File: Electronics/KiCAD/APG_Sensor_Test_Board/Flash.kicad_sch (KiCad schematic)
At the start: 0 parts

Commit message: added flash schematic
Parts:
- added C3: C, symbol Device:C
- added R2: 0, symbol Device:R
- added U?: W25Q128JVS, Package_SO:SOIC-8_5.23x5.23mm_P1.27mm, symbol Memory_Flash:W25Q128JVS
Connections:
- new net +3.3V: R2.1
- new net FCLK: U?.6 (CLK)
- new net FCS: U?.1 (~{CS})
- new net FMISO: U?.2 (DO(IO1))
- new net FMOSI: U?.5 (DI(IO0))
- new net FPWR: C3.1, R2.2, U?.3 (IO2), U?.7 (IO3), U?.8 (VCC)
- new net GND: C3.2, U?.4 (GND)

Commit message: Cleaning up schematics
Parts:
- C3: value C -> 1u
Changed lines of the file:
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@@
 			)
 		)
-		(property "Value" "C"
+		(property "Value" "1u"
 			(at 140.97 54.6099 0)
 			(effects

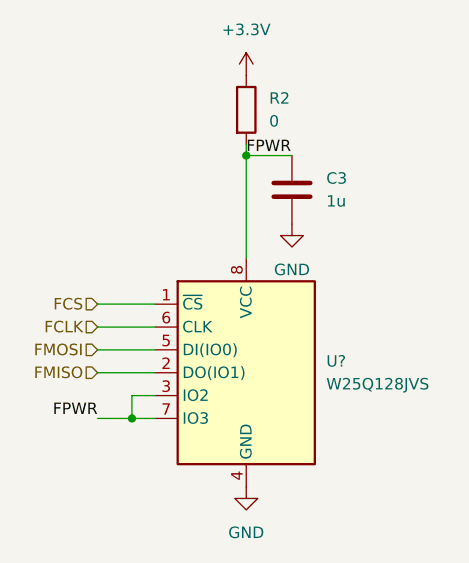
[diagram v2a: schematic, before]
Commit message: Gannon inspection decision to change IMU
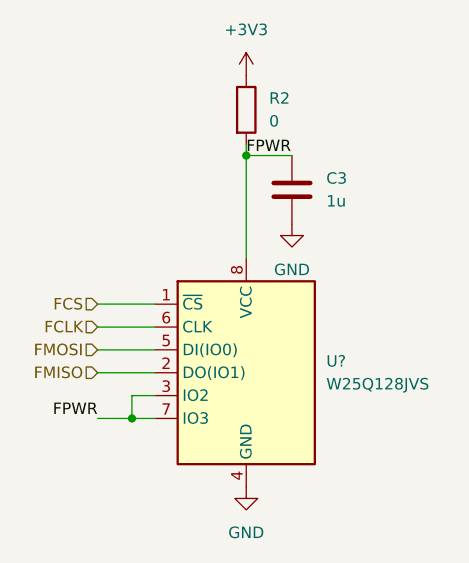
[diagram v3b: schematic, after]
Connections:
- net +3.3V renamed +3V3
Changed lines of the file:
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@@
-	)
-	(symbol
-		(lib_id "power:+3.3V")
-		(at 132.08 40.64 0)
-		(unit 1)
-		(exclude_from_sim no)
-		(in_bom yes)
-		(on_board yes)
-		(dnp no)
-		(fields_autoplaced yes)
-		(property "Reference" "#PWR03"
-			(at 132.08 44.45 0)
-			(effects
-				(font
-					(size 1.27 1.27)
-				)
-				(hide yes)
-			)
-		)
-		(property "Value" "+3.3V"
-			(at 132.08 35.56 0)
-			(effects
-				(font
-					(size 1.27 1.27)
-				)
-			)
-		)
-		(property "Footprint" ""
-			(at 132.08 40.64 0)
-			(effects
-				(font
-					(size 1.27 1.27)
-				)
-				(hide yes)
-			)
-		)
-		(property "Datasheet" ""
-			(at 132.08 40.64 0)
-			(effects
-				(font
-					(size 1.27 1.27)
-				)
-				(hide yes)
-			)
-		)
-		(property "Description" "Power symbol creates a global label with name \"+3.3V\""
-			(at 132.08 40.64 0)
-			(effects
-				(font
-					(size 1.27 1.27)
-				)
-				(hide yes)
-			)
-		)
-		(pin "1"
-		)
-		(instances
-			(project ""
-				(path "/3161be0c-372f-463d-be0a-bab00f344057/1176df13-1d31-4c0d-ab61-bd75d7380dc4"
-					(reference "#PWR03")
-					(unit 1)
-				)
-			)
-		)
 	)
 	(symbol
@@
 					(unit 1)
 				)
+			)
+		)
+	)
+	(symbol
+		(lib_id "power:+3V3")
+		(at 132.08 40.64 0)
+		(unit 1)
+		(exclude_from_sim no)
+		(in_bom yes)
+		(on_board yes)
+		(dnp no)
+		(fields_autoplaced yes)
+		(property "Reference" "#PWR03"
+			(at 132.08 44.45 0)
+			(effects
+				(font
+					(size 1.27 1.27)
+				)
+				(hide yes)
+			)
+		)
+		(property "Value" "+3V3"
+			(at 132.08 35.56 0)
+			(effects
+				(font
+					(size 1.27 1.27)
+				)
+			)
+		)
+		(property "Footprint" ""
+			(at 132.08 40.64 0)
+			(effects
+				(font
+					(size 1.27 1.27)
+				)
+				(hide yes)
+			)
+		)
+		(property "Datasheet" ""
+			(at 132.08 40.64 0)
+			(effects
+				(font
+					(size 1.27 1.27)
+				)
+				(hide yes)
+			)
+		)
+		(property "Description" "Power symbol creates a global label with name \"+3V3\""
+			(at 132.08 40.64 0)
+			(effects
+				(font
+					(size 1.27 1.27)
+				)
+				(hide yes)
+			)
+		)
+		(pin "1"
+		)
+		(instances
+			(project ""
+				(path "/3161be0c-372f-463d-be0a-bab00f344057/1176df13-1d31-4c0d-ab61-bd75d7380dc4"
+					(reference "#PWR03")
+					(unit 1)
+				)

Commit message: reaninotate and begin footprints
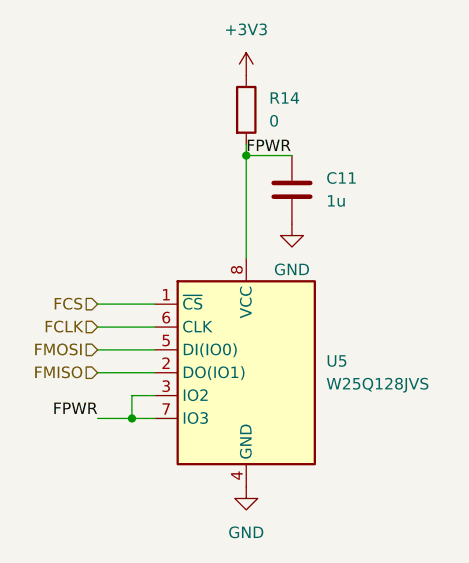
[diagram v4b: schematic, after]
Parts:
- C11: renamed from C3; footprint (none) -> Capacitor_SMD:C_0805_2012Metric
- R14: renamed from R2; footprint (none) -> Resistor_SMD:R_0805_2012Metric
- gave numbers to parts that had none: 1
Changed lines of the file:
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@@
 		(dnp no)
 		(fields_autoplaced yes)
-		(property "Reference" "R2"
+		(property "Reference" "R14"
 			(at 134.62 43.1799 0)
 			(effects
@@
 			)
 		)
-		(property "Footprint" ""
+		(property "Footprint" "Resistor_SMD:R_0805_2012Metric"
 			(at 130.302 44.45 90)
 			(effects
@@
 			(project ""
 				(path "/3161be0c-372f-463d-be0a-bab00f344057/1176df13-1d31-4c0d-ab61-bd75d7380dc4"
-					(reference "R2")
+					(reference "R14")
 					(unit 1)
 				)
@@
 		(dnp no)
 		(fields_autoplaced yes)
-		(property "Reference" "#PWR02"
+		(property "Reference" "#PWR033"
 			(at 132.08 92.71 0)
 			(effects
@@
 			(project ""
 				(path "/3161be0c-372f-463d-be0a-bab00f344057/1176df13-1d31-4c0d-ab61-bd75d7380dc4"
-					(reference "#PWR02")
+					(reference "#PWR033")
 					(unit 1)
 				)
@@
 		(dnp no)
 		(fields_autoplaced yes)
-		(property "Reference" "#PWR03"
+		(property "Reference" "#PWR032"
 			(at 132.08 44.45 0)
 			(effects
@@
 			(project ""
 				(path "/3161be0c-372f-463d-be0a-bab00f344057/1176df13-1d31-4c0d-ab61-bd75d7380dc4"
-					(reference "#PWR03")
+					(reference "#PWR032")
 					(unit 1)
 				)
@@
 		(dnp no)
 		(fields_autoplaced yes)
-		(property "Reference" "#PWR04"
+		(property "Reference" "#PWR034"
 			(at 137.16 63.5 0)
 			(effects
@@
 			(project ""
 				(path "/3161be0c-372f-463d-be0a-bab00f344057/1176df13-1d31-4c0d-ab61-bd75d7380dc4"
-					(reference "#PWR04")
+					(reference "#PWR034")
 					(unit 1)
 				)
@@
 		(dnp no)
 		(fields_autoplaced yes)
-		(property "Reference" "C3"
+		(property "Reference" "C11"
 			(at 140.97 52.0699 0)
 			(effects
@@
 			)
 		)
-		(property "Footprint" ""
+		(property "Footprint" "Capacitor_SMD:C_0805_2012Metric"
 			(at 138.1252 57.15 0)
 			(effects
@@
 			(project ""
 				(path "/3161be0c-372f-463d-be0a-bab00f344057/1176df13-1d31-4c0d-ab61-bd75d7380dc4"
-					(reference "C3")
+					(reference "C11")
 					(unit 1)
 				)
@@
 		(dnp no)
 		(fields_autoplaced yes)
-		(property "Reference" "U?"
+		(property "Reference" "U5"
 			(at 140.97 72.3899 0)
 			(effects
@@
 			(project "APG_Sensor_Test_Board"
 				(path "/3161be0c-372f-463d-be0a-bab00f344057/1176df13-1d31-4c0d-ab61-bd75d7380dc4"
-					(reference "U?")
-					(unit 1)
-				)
+					(reference "U5")
+					(unit 1)
+				)

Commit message: JLC part numbers
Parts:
- U5: JLCPCB (none) -> C97521
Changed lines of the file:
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@@
+			)
+		)
+		(property "JLCPCB" "C97521"
+			(at 132.08 73.66 0)
+			(effects
+				(font
+					(size 1.27 1.27)
+				)
+				(hide yes)
 			)
 		)

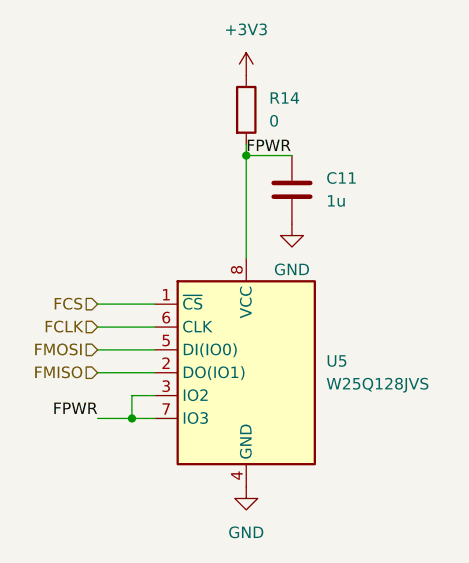
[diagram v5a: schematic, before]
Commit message: MOved IMU and HIGH G to SPI other misc changes
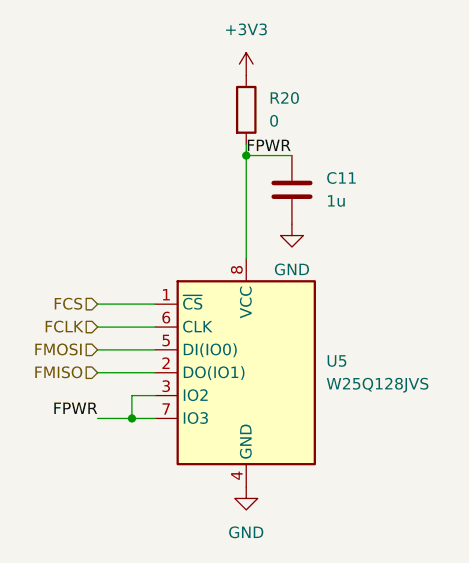
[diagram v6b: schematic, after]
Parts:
- renumbered R14 to R20
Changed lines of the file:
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@@
 		(dnp no)
 		(fields_autoplaced yes)
-		(property "Reference" "R14"
+		(property "Reference" "R20"
 			(at 134.62 43.1799 0)
 			(effects
@@
 			(project ""
 				(path "/3161be0c-372f-463d-be0a-bab00f344057/1176df13-1d31-4c0d-ab61-bd75d7380dc4"
-					(reference "R14")
+					(reference "R20")
 					(unit 1)
 				)
@@
 		(dnp no)
 		(fields_autoplaced yes)
-		(property "Reference" "#PWR033"
+		(property "Reference" "#PWR030"
 			(at 132.08 92.71 0)
 			(effects
@@
 			(project ""
 				(path "/3161be0c-372f-463d-be0a-bab00f344057/1176df13-1d31-4c0d-ab61-bd75d7380dc4"
-					(reference "#PWR033")
+					(reference "#PWR030")
 					(unit 1)
 				)
@@
 		(dnp no)
 		(fields_autoplaced yes)
-		(property "Reference" "#PWR032"
+		(property "Reference" "#PWR029"
 			(at 132.08 44.45 0)
 			(effects
@@
 			(project ""
 				(path "/3161be0c-372f-463d-be0a-bab00f344057/1176df13-1d31-4c0d-ab61-bd75d7380dc4"
-					(reference "#PWR032")
+					(reference "#PWR029")
 					(unit 1)
 				)
@@
 		(dnp no)
 		(fields_autoplaced yes)
-		(property "Reference" "#PWR034"
+		(property "Reference" "#PWR031"
 			(at 137.16 63.5 0)
 			(effects
@@
 			(project ""
 				(path "/3161be0c-372f-463d-be0a-bab00f344057/1176df13-1d31-4c0d-ab61-bd75d7380dc4"
-					(reference "#PWR034")
+					(reference "#PWR031")
 					(unit 1)
 				)
@@
 			(project ""
 				(path "/a3eca312-f18e-4f55-a0dd-dacc05f93778"
-					(reference "U1")
-					(unit 1)
-				)
+					(reference "U?")
+					(unit 1)
+				)

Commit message: Layout and routing
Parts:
- added R31: 10k, Resistor_SMD:R_0603_1608Metric, symbol Device:R
- C11: footprint Capacitor_SMD:C_0805_2012Metric -> Capacitor_SMD:C_0603_1608Metric
- R20: footprint Resistor_SMD:R_0805_2012Metric -> Resistor_SMD:R_0603_1608Metric
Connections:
- net FCS: now also R31.2
- net FPWR: now also R31.1
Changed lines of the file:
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@@
 		(color 0 0 0 0)
 	)
+	(junction
+		(at 116.84 66.04)
+		(diameter 0)
+		(color 0 0 0 0)
+	)
 	(wire
 		(pts
@@
 	(wire
 		(pts
-			(xy 115.57 66.04) (xy 121.92 66.04)
+			(xy 115.57 66.04) (xy 116.84 66.04)
 		)
 		(stroke
@@
 	(wire
 		(pts
+			(xy 116.84 60.96) (xy 116.84 66.04)
+		)
+		(stroke
+			(width 0)
+			(type default)
+		)
+	)
+	(wire
+		(pts
 			(xy 115.57 68.58) (xy 121.92 68.58)
 		)
@@
 	(wire
 		(pts
+			(xy 116.84 66.04) (xy 121.92 66.04)
+		)
+		(stroke
+			(width 0)
+			(type default)
+		)
+	)
+	(wire
+		(pts
 			(xy 115.57 78.74) (xy 119.38 78.74)
 		)
@@
 			(width 0)
 			(type default)
+		)
+	)
+	(label "FPWR"
+		(at 116.84 53.34 0)
+		(fields_autoplaced yes)
+		(effects
+			(font
+				(size 1.27 1.27)
+			)
+			(justify left bottom)
 		)
 	)
@@
 			)
 		)
-		(property "Footprint" "Resistor_SMD:R_0805_2012Metric"
+		(property "Footprint" "Resistor_SMD:R_0603_1608Metric"
 			(at 130.302 44.45 90)
 			(effects
@@
 	)
 	(symbol
+		(lib_id "Device:R")
+		(at 116.84 57.15 0)
+		(unit 1)
+		(exclude_from_sim no)
+		(in_bom yes)
+		(on_board yes)
+		(dnp no)
+		(fields_autoplaced yes)
+		(property "Reference" "R31"
+			(at 119.38 55.8799 0)
+			(effects
+				(font
+					(size 1.27 1.27)
+				)
+				(justify left)
+			)
+		)
+		(property "Value" "10k"
+			(at 119.38 58.4199 0)
+			(effects
+				(font
+					(size 1.27 1.27)
+				)
+				(justify left)
+			)
+		)
+		(property "Footprint" "Resistor_SMD:R_0603_1608Metric"
+			(at 115.062 57.15 90)
+			(effects
+				(font
+					(size 1.27 1.27)
+				)
+				(hide yes)
+			)
+		)
+		(property "Datasheet" "~"
+			(at 116.84 57.15 0)
+			(effects
+				(font
+					(size 1.27 1.27)
+				)
+				(hide yes)
+			)
+		)
+		(property "Description" "Resistor"
+			(at 116.84 57.15 0)
+			(effects
+				(font
+					(size 1.27 1.27)
+				)
+				(hide yes)
+			)
+		)
+		(pin "2"
+		)
+		(pin "1"
+		)
+		(instances
+			(project "APG_Sensor_Test_Board"
+				(path "/3161be0c-372f-463d-be0a-bab00f344057/1176df13-1d31-4c0d-ab61-bd75d7380dc4"
+					(reference "R31")
+					(unit 1)
+				)
+			)
+		)
+	)
+	(symbol
 		(lib_id "power:GND")
 		(at 137.16 57.15 0)
@@
 			)
 		)
-		(property "Footprint" "Capacitor_SMD:C_0805_2012Metric"
+		(property "Footprint" "Capacitor_SMD:C_0603_1608Metric"
 			(at 138.1252 57.15 0)
 			(effects

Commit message: APG Sensor Board V1.1 Production
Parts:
- C11: value 1u -> 1uF
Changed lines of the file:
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@@
 			)
 		)
-		(property "Value" "1u"
+		(property "Value" "1uF"
 			(at 140.97 54.6099 0)
 			(effects
